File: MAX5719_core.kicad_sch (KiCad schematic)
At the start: 27 parts, among them J16 Conn_Coaxial, J23 Conn_Coaxial, U10 ADA4841-2, U21 MAX5719xSD, U8 MAX5719xSD

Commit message: Analog section complete!
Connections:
- net VDD is gone; now on net +5VA: C92.1, U10.8 (V+)
- net DAC2_output: now reaches J23.1 (In), R121.2
- net DAC_Ref renamed Ref_Buf
- net VSS renamed -5VA
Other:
- moved on the sheet: R119
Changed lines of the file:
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@@
   (junction (at 238.76 67.31) (diameter 0) (color 0 0 0 0)
   )
+  (junction (at 161.29 118.11) (diameter 0) (color 0 0 0 0)
+  )
   (junction (at 87.63 64.77) (diameter 0) (color 0 0 0 0)
   )
@@
     (stroke (width 0) (type default) (color 0 0 0 0))
   )
-  (wire (pts (xy 147.32 113.03) (xy 147.32 132.08))
+  (wire (pts (xy 147.32 109.22) (xy 147.32 132.08))
     (stroke (width 0) (type default) (color 0 0 0 0))
   )
@@
     (stroke (width 0) (type default) (color 0 0 0 0))
   )
-  (wire (pts (xy 160.02 118.11) (xy 163.83 118.11))
+  (wire (pts (xy 160.02 118.11) (xy 161.29 118.11))
     (stroke (width 0) (type default) (color 0 0 0 0))
   )
@@
     (stroke (width 0) (type default) (color 0 0 0 0))
   )
+  (wire (pts (xy 161.29 109.22) (xy 161.29 118.11))
+    (stroke (width 0) (type default) (color 0 0 0 0))
+  )
   (wire (pts (xy 69.85 41.91) (xy 69.85 44.45))
     (stroke (width 0) (type default) (color 0 0 0 0))
@@
     (stroke (width 0) (type default) (color 0 0 0 0))
   )
+  (wire (pts (xy 161.29 118.11) (xy 163.83 118.11))
+    (stroke (width 0) (type default) (color 0 0 0 0))
+  )
   (wire (pts (xy 77.47 99.06) (xy 73.66 99.06))
     (stroke (width 0) (type default) (color 0 0 0 0))
@@
     (stroke (width 0) (type default) (color 0 0 0 0))
   )
-  (wire (pts (xy 147.32 105.41) (xy 147.32 96.52))
+  (wire (pts (xy 147.32 101.6) (xy 147.32 96.52))
     (stroke (width 0) (type default) (color 0 0 0 0))
   )
@@
     (effects (font (size 1.27 1.27)) (justify left bottom))
   )
-  (label "DAC_Ref" (at 52.07 41.91 0)
-    (effects (font (size 1.27 1.27)) (justify left bottom))
-  )
-  (label "DAC_Ref" (at 45.72 107.95 0)
-    (effects (font (size 1.27 1.27)) (justify left bottom))
+  (global_label "Ref_Buf" (shape input) (at 45.72 107.95 180) (fields_autoplaced)
+    (effects (font (size 1.27 1.27)) (justify right))
+    (property "Intersheet References" "${INTERSHEET_REFS}" (id 0) (at 36.1102 108.0294 0)
+      (effects (font (size 1.27 1.27)) (justify right) hide)
+    )
   )
   (global_label "DAC2_LDAC" (shape input) (at 71.12 123.19 180) (fields_autoplaced)
@@
     )
   )
+  (global_label "DAC2_output" (shape input) (at 161.29 109.22 90) (fields_autoplaced)
+    (effects (font (size 1.27 1.27)) (justify left))
+    (property "Intersheet References" "${INTERSHEET_REFS}" (id 0) (at 161.3694 94.9536 90)
+      (effects (font (size 1.27 1.27)) (justify left) hide)
+    )
+  )
   (global_label "DAC1_LDAC" (shape input) (at 71.12 57.15 180) (fields_autoplaced)
     (effects (font (size 1.27 1.27)) (justify right))
@@
     )
   )
+  (global_label "Ref_Buf" (shape input) (at 52.07 41.91 180) (fields_autoplaced)
+    (effects (font (size 1.27 1.27)) (justify right))
+    (property "Intersheet References" "${INTERSHEET_REFS}" (id 0) (at 42.4602 41.9894 0)
+      (effects (font (size 1.27 1.27)) (justify right) hide)
+    )
+  )
   (global_label "DAC2_CS" (shape input) (at 71.12 115.57 180) (fields_autoplaced)
     (effects (font (size 1.27 1.27)) (justify right))
@@
     (pin "2")
   )
-  (symbol (lib_id "power:VDD") (at 238.76 64.77 0) (unit 1)
-    (in_bom yes) (on_board yes) (fields_autoplaced)
-    (property "Reference" "#PWR026" (id 0) (at 238.76 68.58 0)
-      (effects (font (size 1.27 1.27)) hide)
-    )
-    (property "Value" "VDD" (id 1) (at 238.76 59.69 0))
-    (property "Footprint" "" (id 2) (at 238.76 64.77 0)
-      (effects (font (size 1.27 1.27)) hide)
-    )
-    (property "Datasheet" "" (id 3) (at 238.76 64.77 0)
-      (effects (font (size 1.27 1.27)) hide)
-    )
-    (pin "1")
-  )
   (symbol (lib_id "power:+5VA") (at 87.63 96.52 0) (unit 1)
     (in_bom yes) (on_board yes) (fields_autoplaced)
@@
     (pin "1")
   )
-  (symbol (lib_id "Device:R") (at 147.32 109.22 0) (mirror y) (unit 1)
-    (in_bom yes) (on_board yes) (fields_autoplaced)
-    (property "Reference" "R119" (id 0) (at 149.86 107.9499 0)
+  (symbol (lib_id "Device:R") (at 147.32 105.41 0) (mirror y) (unit 1)
+    (in_bom yes) (on_board yes) (fields_autoplaced)
+    (property "Reference" "R119" (id 0) (at 149.86 104.1399 0)
       (effects (font (size 1.27 1.27)) (justify right))
     )
-    (property "Value" "100" (id 1) (at 149.86 110.4899 0)
+    (property "Value" "100" (id 1) (at 149.86 106.6799 0)
       (effects (font (size 1.27 1.27)) (justify right))
     )
-    (property "Footprint" "Resistor_SMD:R_0805_2012Metric" (id 2) (at 149.098 109.22 90)
-      (effects (font (size 1.27 1.27)) hide)
-    )
-    (property "Datasheet" "~" (id 3) (at 147.32 109.22 0)
+    (property "Footprint" "Resistor_SMD:R_0805_2012Metric" (id 2) (at 149.098 105.41 90)
+      (effects (font (size 1.27 1.27)) hide)
+    )
+    (property "Datasheet" "~" (id 3) (at 147.32 105.41 0)
       (effects (font (size 1.27 1.27)) hide)
     )
@@
     (pin "8")
   )
-  (symbol (lib_id "power:VSS") (at 238.76 95.25 180) (unit 1)
-    (in_bom yes) (on_board yes) (fields_autoplaced)
-    (property "Reference" "#PWR027" (id 0) (at 238.76 91.44 0)
-      (effects (font (size 1.27 1.27)) hide)
-    )
-    (property "Value" "VSS" (id 1) (at 238.76 100.33 0))
-    (property "Footprint" "" (id 2) (at 238.76 95.25 0)
-      (effects (font (size 1.27 1.27)) hide)
-    )
-    (property "Datasheet" "" (id 3) (at 238.76 95.25 0)
-      (effects (font (size 1.27 1.27)) hide)
-    )
-    (pin "1")
-  )
   (symbol (lib_id "Device:C") (at 81.28 33.02 270) (unit 1)
     (in_bom yes) (on_board yes)
@@
     (pin "2")
     (pin "3")
+  )
+  (symbol (lib_id "power:-5VA") (at 238.76 95.25 180) (unit 1)
+    (in_bom yes) (on_board yes) (fields_autoplaced)
+    (property "Reference" "#PWR0238" (id 0) (at 238.76 97.79 0)
+      (effects (font (size 1.27 1.27)) hide)
+    )
+    (property "Value" "-5VA" (id 1) (at 238.76 100.33 0))
+    (property "Footprint" "" (id 2) (at 238.76 95.25 0)
+      (effects (font (size 1.27 1.27)) hide)
+    )
+    (property "Datasheet" "" (id 3) (at 238.76 95.25 0)
+      (effects (font (size 1.27 1.27)) hide)
+    )
+    (pin "1")
   )
   (symbol (lib_id "power:GNDA") (at 87.63 132.08 0) (unit 1)
@@
       (effects (font (size 1.27 1.27)) hide)
     )
+    (pin "1")
+  )
+  (symbol (lib_id "power:+5VA") (at 238.76 64.77 0) (unit 1)
+    (in_bom yes) (on_board yes)
+    (property "Reference" "#PWR0239" (id 0) (at 238.76 68.58 0)
+      (effects (font (size 1.27 1.27)) hide)
+    )
+    (property "Value" "+5VA" (id 1) (at 238.76 59.69 0))
+    (property "Footprint" "" (id 2) (at 238.76 64.77 0)
+      (effects (font (size 1.27 1.27)) hide)
+    )
+    (property "Datasheet" "" (id 3) (at 238.76 64.77 0)
+      (effects (font (size 1.27 1.27)) hide)
+    )

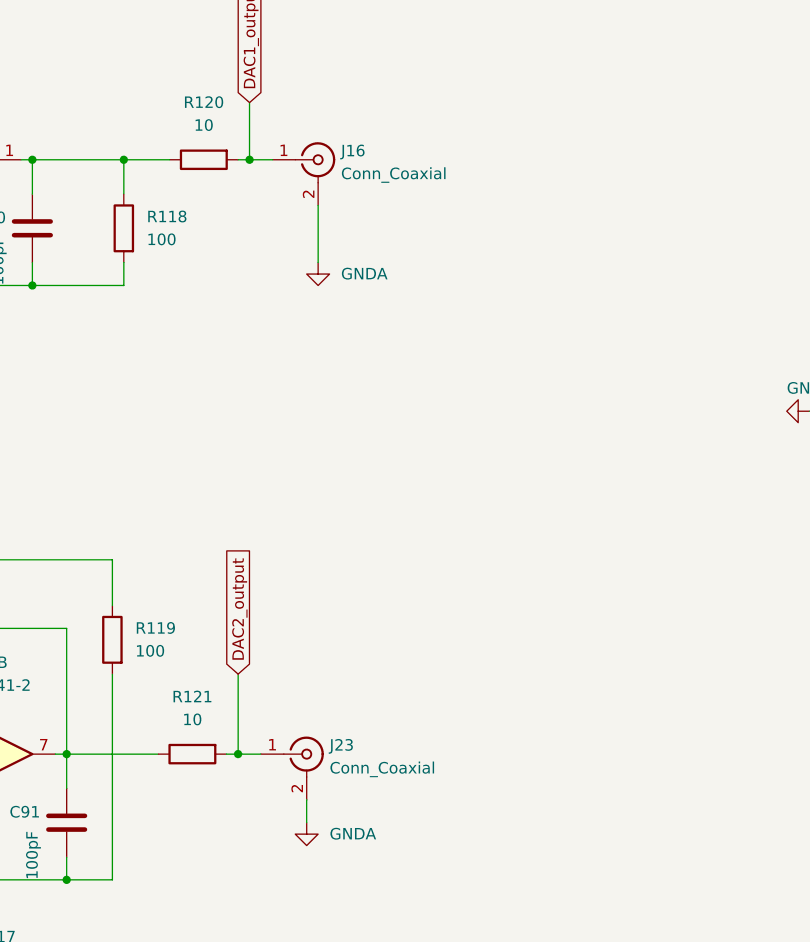
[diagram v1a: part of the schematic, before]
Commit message: Version 1.0 submitted to JLCPCB
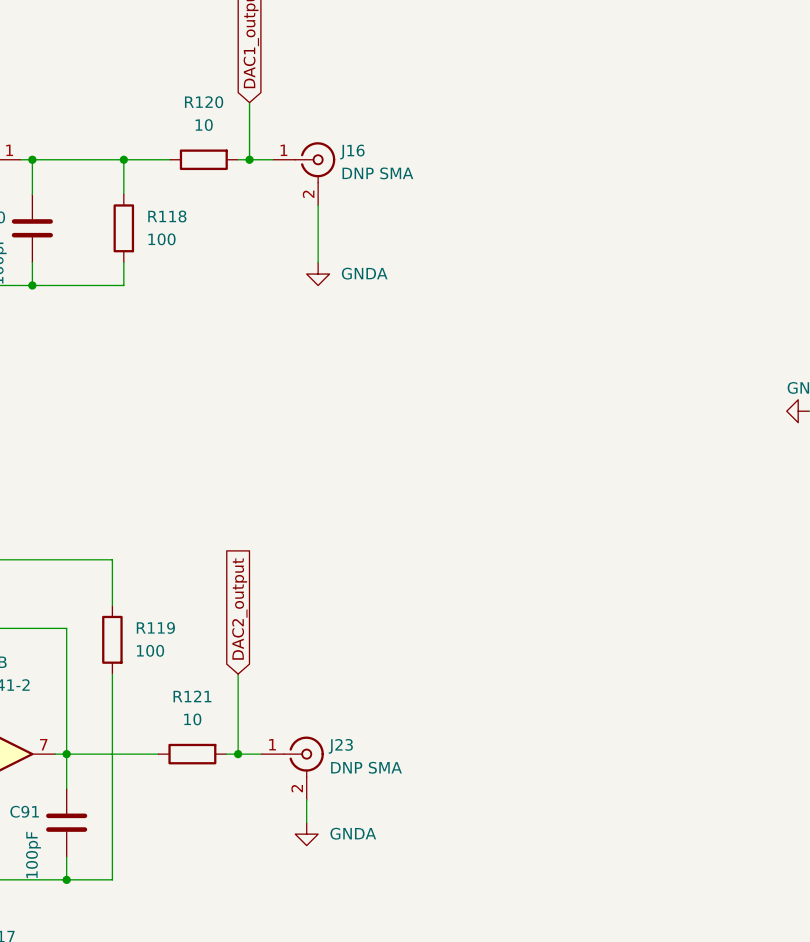
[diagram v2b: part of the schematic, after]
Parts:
- J16, J23: value Conn_Coaxial -> DNP SMA
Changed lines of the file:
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@@
       (effects (font (size 1.27 1.27)) (justify left))
     )
-    (property "Value" "Conn_Coaxial" (id 1) (at 171.45 119.6731 0)
+    (property "Value" "DNP SMA" (id 1) (at 171.45 119.6731 0)
       (effects (font (size 1.27 1.27)) (justify left))
     )
@@
       (effects (font (size 1.27 1.27)) (justify left))
     )
-    (property "Value" "Conn_Coaxial" (id 1) (at 172.72 53.6331 0)
-      (effects (font (size 1.27 1.27)) (justify left))
-    )
+    (property "Value" "DNP SMA" (id 1) (at 172.72 53.6331 0)
+      (effects (font (size 1.27 1.27)) (justify left))
+    )
